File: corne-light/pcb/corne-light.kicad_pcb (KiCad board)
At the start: 2 copper layers, 275.5 x 105.6 mm, 122 parts, among them J1 MJ-4PP-9, J2 OLED, J5 Breakaway_Tabs, J6 MJ-4PP-9, J7 OLED, SW1 SW_PUSH, SW10 SW_PUSH, SW11 SW_PUSH, SW12 SW_PUSH, SW13 SW_PUSH, SW14 SW_PUSH, SW15 SW_PUSH, SW16 SW_PUSH, SW17 SW_PUSH, SW18 SW_PUSH, SW19 SW_PUSH, SW2 SW_PUSH, SW20 SW_PUSH, SW21 SW_PUSH, SW22 SW_PUSH, SW23 SW_PUSH, SW24 SW_PUSH, SW25 SW_PUSH, SW26 SW_PUSH, SW27 SW_PUSH, SW28 SW_PUSH, SW29 SW_PUSH, SW3 SW_PUSH, SW30 SW_PUSH, SW31 SW_PUSH, SW32 SW_PUSH, SW33 SW_PUSH, SW34 SW_PUSH, SW35 SW_PUSH, SW36 SW_PUSH, SW37 SW_PUSH, SW38 SW_PUSH, SW39 SW_PUSH, SW4 SW_PUSH, SW40 SW_PUSH, SW41 SW_PUSH, SW42 SW_PUSH, SW5 SW_PUSH, SW6 SW_PUSH, SW7 SW_PUSH, SW8 SW_PUSH, SW9 SW_PUSH, U1 ProMicro, U2 ProMicro

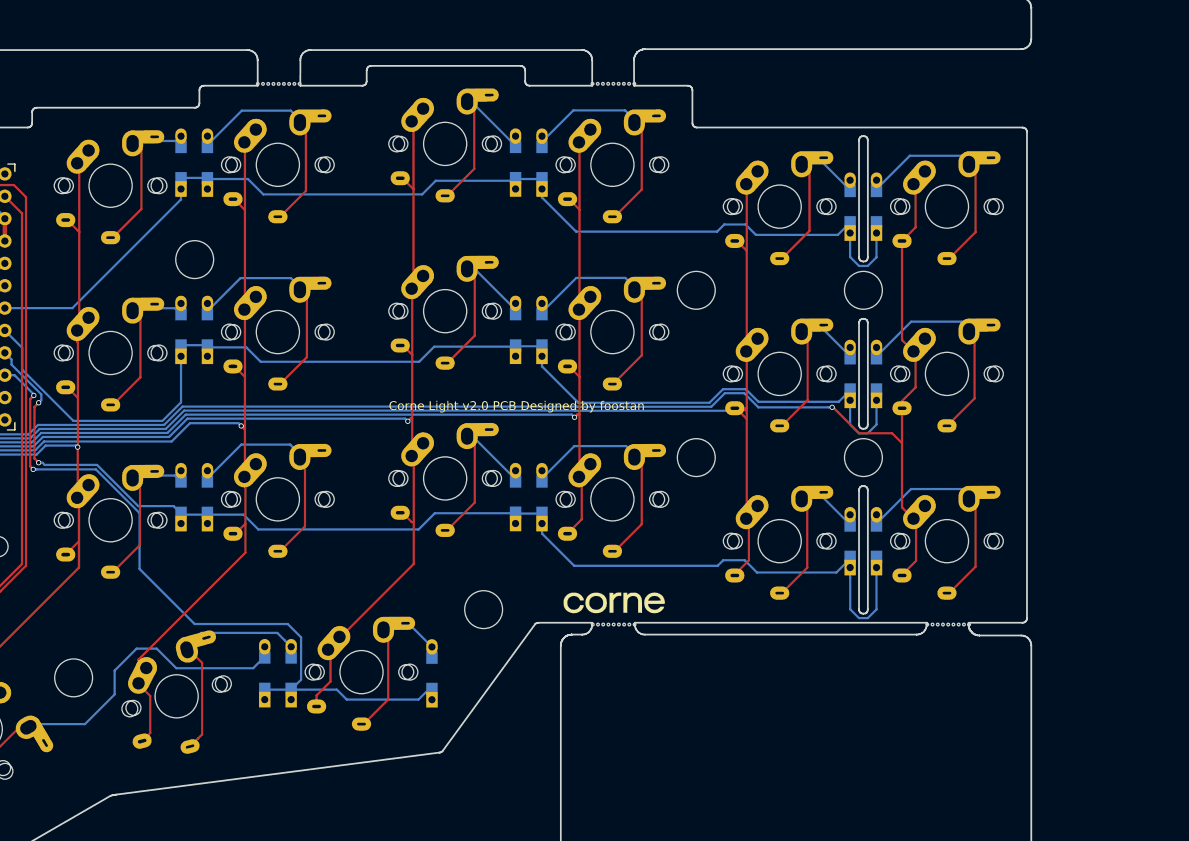
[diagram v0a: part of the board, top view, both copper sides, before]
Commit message: Update corne-light.kicad_pcb
gombok jó helyen
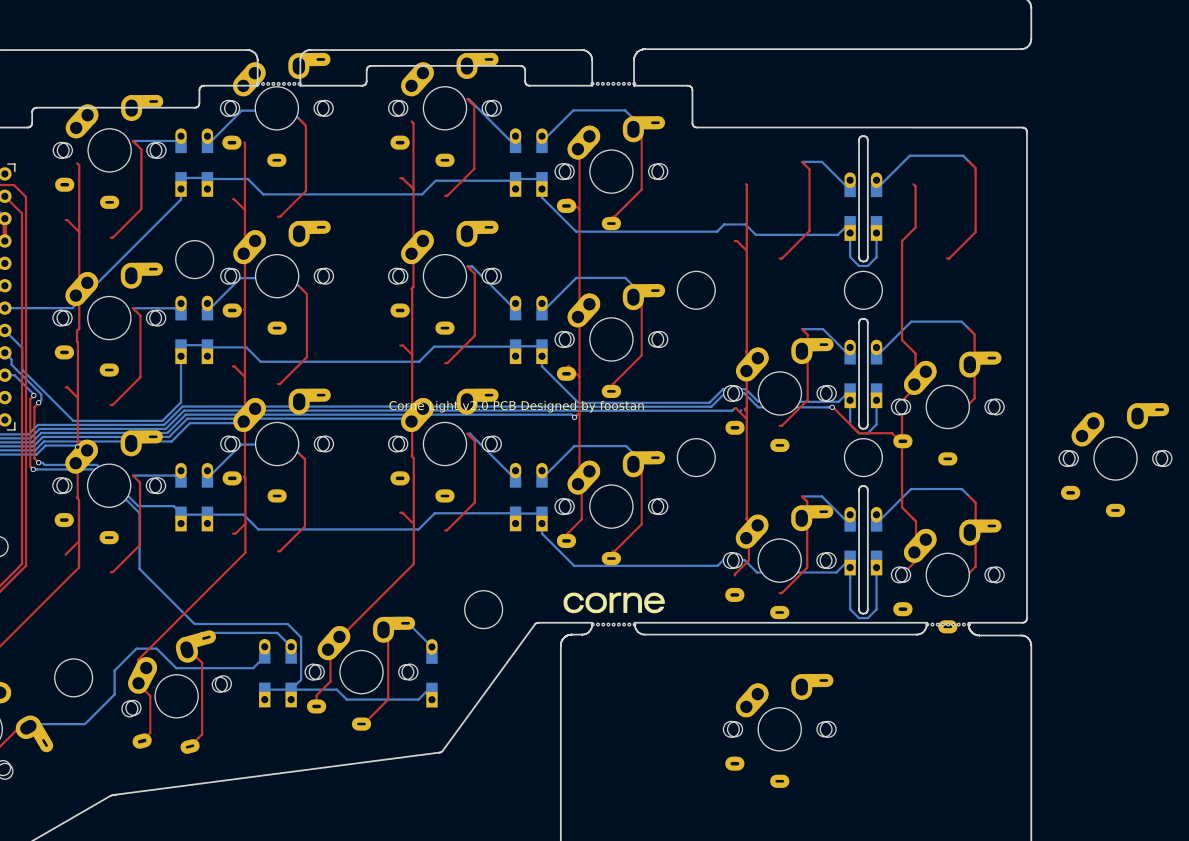
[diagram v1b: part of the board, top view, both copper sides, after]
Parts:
- moved SW28 22.8 mm to (278.8, 87.7)
- moved SW22 22.8 mm to (278.8, 68.7)
- moved SW35 21.4 mm to (259.7, 105.3)
- moved SW34 21.3 mm to (297.8, 74.5)
- moved SW23 21.2 mm to (259.7, 67.1)
- moved SW29 21.2 mm to (259.7, 86.1)
- moved SW26 6.41 mm to (202.6, 34.8)
- moved SW32 6.35 mm to (202.6, 53.8)
- moved SW38 6.29 mm to (202.6, 72.9)
- moved SW25 4.04 mm to (221.7, 34.8)
- moved SW27 4.01 mm to (183.6, 39.5)
- moved SW31 3.98 mm to (221.7, 53.8)
- moved SW33 3.97 mm to (183.5, 58.6)
- moved SW39 3.93 mm to (183.5, 77.6)
- moved SW37 3.91 mm to (221.7, 72.9)
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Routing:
- net (no net): track 0.00 -> 26.5 mm
- net Net-(D34-Pad2): track 27.2 -> 13.9 mm
- net Net-(D28-Pad2): track 27.0 -> 13.9 mm
